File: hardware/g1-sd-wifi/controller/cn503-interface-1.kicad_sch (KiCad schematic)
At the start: 2 parts, among them J50 FH12-20S-0.5SH(55), J51 FH12-20S-0.5SH(55)

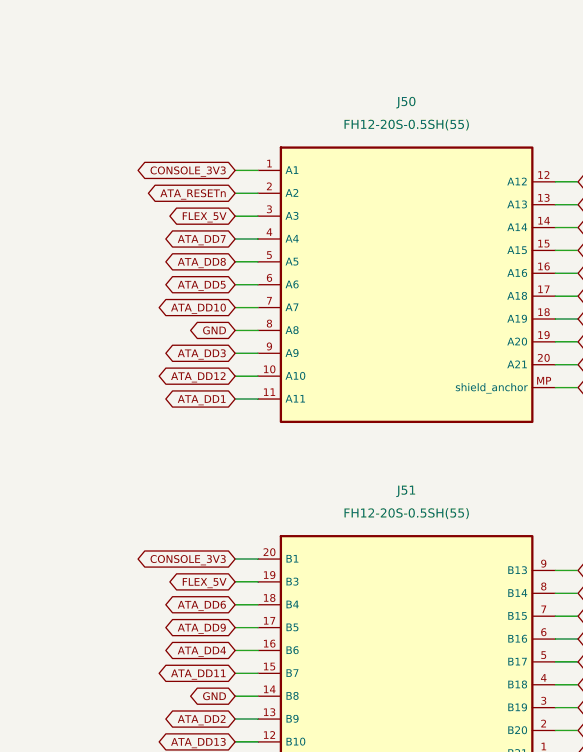
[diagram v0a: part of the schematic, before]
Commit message: G1 safety: fuse the host 3.3-V entry; no console 5 V on the flex or carrier
Host 3.3 V reached about 30 carrier parts straight from two flex contacts,
and the two console-5-V contacts were joined by an unused carrier trace;
a short on either would load a console supply through 0.5 A connector
contacts with no fuse anywhere. Now:

- F21 (0467.500NR, 0.5 A fast, same 467 family as F20) sits between the one
  remaining 3.3-V entry, J51 B1, and CONSOLE_3V3. If it opens the buffers
  lose VCCB and isolate, and U25 reports the host rail absent.
- CN503 A1 (second 3.3 V) and A3/B3 (5 V) get no flex copper at all: no
  landing pad, no trace, only an unconnected mating finger, so a chafed
  flex cannot short a console supply. Their carrier socket pins are bare.
  flex-interface.json lists them; the flex and carrier generators and both
  checks read that list. Flex ERC/DRC/parity 0; carrier ERC 0, integration
  check pass (362 parts).
- The DSN export keeps the 5-V and storage supply nets on the 1 oz outer
  layers: on 0.5 oz inner copper a 0.25 mm track at the fuse current would
  overheat (IPC-2221).
- F21 is placed by the floorplan next to J51; board DRC 0, parity 0
  (unrouted).

Co-Authored-By: Claude Opus 5.5 <noreply@anthropic.com>
Claude-Session: https://claude.ai/code/session_01Gp9EYc2r9fMpZ7V8WtfonZ
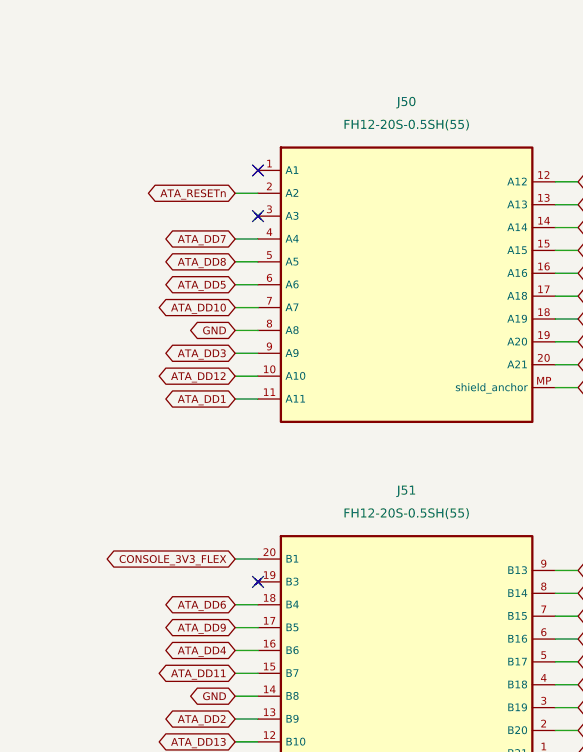
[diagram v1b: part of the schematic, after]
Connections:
- net CONSOLE_3V3: no longer names the net of J50.1 (A1)
- net CONSOLE_3V3: no longer J51.20 (B1)
- net FLEX_5V: no longer names the net of J50.3 (A3)
- net FLEX_5V: no longer J51.19 (B3)
- new net CONSOLE_3V3_FLEX: J51.20 (B1)
- no-connect marks 0 -> 3
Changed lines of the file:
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@@
  (pin "MP")
  (instances (project "KUI-G1-Bridge-RevA" (path "/8477501f-fac0-5337-89a1-fc3585ab7e6e/927d1b8a-d096-52bc-9740-e908cdee7842" (reference "J50") (unit 1)))) )
- (wire (pts (xy 39.37 39.37) (xy 36.83 39.37)) (stroke (width 0) (type default)))
-(global_label "CONSOLE_3V3" (shape bidirectional) (at 36.83 39.37 0) (effects (font (size 0.85 0.85)) (justify right)))
+ (no_connect (at 39.37 39.37))
  (wire (pts (xy 39.37 41.91) (xy 36.83 41.91)) (stroke (width 0) (type default)))
 (global_label "ATA_RESETn" (shape bidirectional) (at 36.83 41.91 0) (effects (font (size 0.85 0.85)) (justify right)))
- (wire (pts (xy 39.37 44.45) (xy 36.83 44.45)) (stroke (width 0) (type default)))
-(global_label "FLEX_5V" (shape bidirectional) (at 36.83 44.45 0) (effects (font (size 0.85 0.85)) (justify right)))
+ (no_connect (at 39.37 44.45))
  (wire (pts (xy 39.37 46.99) (xy 36.83 46.99)) (stroke (width 0) (type default)))
 (global_label "ATA_DD7" (shape bidirectional) (at 36.83 46.99 0) (effects (font (size 0.85 0.85)) (justify right)))
@@
  (instances (project "KUI-G1-Bridge-RevA" (path "/8477501f-fac0-5337-89a1-fc3585ab7e6e/927d1b8a-d096-52bc-9740-e908cdee7842" (reference "J51") (unit 1)))) )
  (wire (pts (xy 39.37 82.55) (xy 36.83 82.55)) (stroke (width 0) (type default)))
-(global_label "CONSOLE_3V3" (shape bidirectional) (at 36.83 82.55 0) (effects (font (size 0.85 0.85)) (justify right)))
- (wire (pts (xy 39.37 85.09) (xy 36.83 85.09)) (stroke (width 0) (type default)))
-(global_label "FLEX_5V" (shape bidirectional) (at 36.83 85.09 0) (effects (font (size 0.85 0.85)) (justify right)))
+(global_label "CONSOLE_3V3_FLEX" (shape bidirectional) (at 36.83 82.55 0) (effects (font (size 0.85 0.85)) (justify right)))
+ (no_connect (at 39.37 85.09))
  (wire (pts (xy 39.37 87.63) (xy 36.83 87.63)) (stroke (width 0) (type default)))
 (global_label "ATA_DD6" (shape bidirectional) (at 36.83 87.63 0) (effects (font (size 0.85 0.85)) (justify right)))
